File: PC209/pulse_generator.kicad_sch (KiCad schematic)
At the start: 33 parts, among them Q1 BC848W, Q2 BC848W, Q3 BC848W, Q4 BC848W, Q5 BC848W, Q6 BC848W, Q7 BC848W

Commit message: PC209: Initial layout for pulse generator sections
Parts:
- TP1, TP3: footprint TestPoint:TestPoint_Keystone_5015_Micro-Minature -> TestPoint:TestPoint_THTPad_2.0x2.0mm_Drill1.0mm; now left out of the parts list
- TP2: value 10 us delay -> 10 μs delay; footprint TestPoint:TestPoint_Keystone_5015_Micro-Minature -> TestPoint:TestPoint_THTPad_2.0x2.0mm_Drill1.0mm; now left out of the parts list
- TP4: value 10 us delay -> 100 μs pulse; footprint TestPoint:TestPoint_Keystone_5015_Micro-Minature -> TestPoint:TestPoint_THTPad_2.0x2.0mm_Drill1.0mm; now left out of the parts list
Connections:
- net Output: now also TP4.1
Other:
- note added: "10 μs Delay"
- note added: "100 μs Pulse"
- note removed: "10 us Delay"
- note removed: "100 us Pulse"
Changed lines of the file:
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@@
+    (stroke (width 0) (type default) (color 0 0 0 0))
+  )
+  (wire (pts (xy 104.14 104.14) (xy 104.14 110.49))
     (stroke (width 0) (type default) (color 0 0 0 0))
   )
@@
     (stroke (width 0) (type default) (color 0 0 0 0))
   )
-  (text "10 us Delay" (at 52.07 31.75 0)
+  (text "10 μs Delay" (at 52.07 31.75 0)
     (effects (font (size 3 3)) (justify left bottom))
   )
-  (text "100 us Pulse" (at 52.07 95.25 0)
+  (text "100 μs Pulse" (at 52.07 95.25 0)
     (effects (font (size 3 3)) (justify left bottom))
   )
@@
   )
   (symbol (lib_id "Connector:TestPoint") (at 46.99 58.42 0) (unit 1)
-    (in_bom yes) (on_board yes)
+    (in_bom no) (on_board yes)
     (property "Reference" "TP1" (id 0) (at 44.45 57.15 90)
       (effects (font (size 1.27 1.27)) (justify left))
@@
       (effects (font (size 1.27 1.27)) (justify left bottom))
     )
-    (property "Footprint" "TestPoint:TestPoint_Keystone_5015_Micro-Minature" (id 2) (at 52.07 58.42 0)
+    (property "Footprint" "TestPoint:TestPoint_THTPad_2.0x2.0mm_Drill1.0mm" (id 2) (at 52.07 58.42 0)
       (effects (font (size 1.27 1.27)) hide)
     )
@@
   )
   (symbol (lib_id "Connector:TestPoint") (at 104.14 104.14 0) (unit 1)
-    (in_bom yes) (on_board yes)
+    (in_bom no) (on_board yes)
     (property "Reference" "TP4" (id 0) (at 101.6 102.87 90)
       (effects (font (size 1.27 1.27)) (justify left))
     )
-    (property "Value" "10 us delay" (id 1) (at 106.68 102.87 90)
+    (property "Value" "100 μs pulse" (id 1) (at 106.68 102.87 90)
       (effects (font (size 1.27 1.27)) (justify left bottom))
     )
-    (property "Footprint" "TestPoint:TestPoint_Keystone_5015_Micro-Minature" (id 2) (at 109.22 104.14 0)
+    (property "Footprint" "TestPoint:TestPoint_THTPad_2.0x2.0mm_Drill1.0mm" (id 2) (at 109.22 104.14 0)
       (effects (font (size 1.27 1.27)) hide)
     )
@@
   )
   (symbol (lib_id "Connector:TestPoint") (at 101.6 54.61 0) (unit 1)
-    (in_bom yes) (on_board yes)
+    (in_bom no) (on_board yes)
     (property "Reference" "TP3" (id 0) (at 99.06 53.34 90)
       (effects (font (size 1.27 1.27)) (justify left))
@@
       (effects (font (size 1.27 1.27)) (justify left bottom))
     )
-    (property "Footprint" "TestPoint:TestPoint_Keystone_5015_Micro-Minature" (id 2) (at 106.68 54.61 0)
+    (property "Footprint" "TestPoint:TestPoint_THTPad_2.0x2.0mm_Drill1.0mm" (id 2) (at 106.68 54.61 0)
       (effects (font (size 1.27 1.27)) hide)
     )
@@
   )
   (symbol (lib_id "Connector:TestPoint") (at 57.15 101.6 270) (unit 1)
-    (in_bom yes) (on_board yes)
+    (in_bom no) (on_board yes)
     (property "Reference" "TP2" (id 0) (at 58.42 99.06 90)
       (effects (font (size 1.27 1.27)) (justify left))
     )
-    (property "Value" "10 us delay" (id 1) (at 58.42 104.14 90)
+    (property "Value" "10 μs delay" (id 1) (at 58.42 104.14 90)
       (effects (font (size 1.27 1.27)) (justify left bottom))
     )
-    (property "Footprint" "TestPoint:TestPoint_Keystone_5015_Micro-Minature" (id 2) (at 57.15 106.68 0)
-      (effects (font (size 1.27 1.27)) hide)
-    )
+    (property "Footprint" "TestPoint:TestPoint_THTPad_2.0x2.0mm_Drill1.0mm" (id 2) (at 57.15 106.68 0)
+      (effects (font (size 1.27 1.27)) hide)
+    )

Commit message: PC209: Rev 1.0
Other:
- company: (none) -> Peter Farley
- title: (none) -> PC209 Pulse Generator
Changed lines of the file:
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@@
 (kicad_sch (version 20211123) (generator eeschema)
   (paper "A4")
+  (title_block
+    (title "PC209 Pulse Generator")
+    (date "2023-01-16")
+    (rev "1.0")
+    (company "Peter Farley")
+    (comment 1 "Rev 1.0: Initial Design")
+  )
   (junction (at 83.82 113.03) (diameter 0) (color 0 0 0 0)
   )
@@
     (stroke (width 0) (type default) (color 0 0 0 0))
   )
-  (wire (pts (xy 26.67 21.59) (xy 29.21 21.59))
-    (stroke (width 0) (type default) (color 0 0 0 0))
-  )
   (wire (pts (xy 67.31 57.15) (xy 67.31 58.42))
     (stroke (width 0) (type default) (color 0 0 0 0))
@@
     (stroke (width 0) (type default) (color 0 0 0 0))
   )
-  (wire (pts (xy 29.21 19.05) (xy 26.67 19.05))
-    (stroke (width 0) (type default) (color 0 0 0 0))
-  )
   (wire (pts (xy 104.14 110.49) (xy 111.76 110.49))
     (stroke (width 0) (type default) (color 0 0 0 0))
@@
   )
   (wire (pts (xy 57.15 63.5) (xy 59.69 63.5))
-    (stroke (width 0) (type default) (color 0 0 0 0))
-  )
-  (wire (pts (xy 29.21 24.13) (xy 26.67 24.13))
     (stroke (width 0) (type default) (color 0 0 0 0))
   )
@@
     (effects (font (size 3 3)) (justify left bottom))
   )
-  (hierarchical_label "GND" (shape input) (at 26.67 24.13 180)
-    (effects (font (size 1.27 1.27)) (justify right))
-  )
   (hierarchical_label "Output" (shape output) (at 153.67 130.81 0)
     (effects (font (size 1.27 1.27)) (justify left))
   )
-  (hierarchical_label "3.6 V" (shape input) (at 26.67 21.59 180)
-    (effects (font (size 1.27 1.27)) (justify right))
-  )
   (hierarchical_label "Input" (shape input) (at 41.91 63.5 180)
-    (effects (font (size 1.27 1.27)) (justify right))
-  )
-  (hierarchical_label "15 V" (shape input) (at 26.67 19.05 180)
     (effects (font (size 1.27 1.27)) (justify right))
   )
@@
     (pin "2")
   )
-  (symbol (lib_id "lib_symbols:+3.6V") (at 29.21 21.59 270) (unit 1)
-    (in_bom yes) (on_board yes) (fields_autoplaced)
-    (property "Reference" "#PWR0118" (id 0) (at 25.4 21.59 0)
-      (effects (font (size 1.27 1.27)) hide)
-    )
-    (property "Value" "+3.6V" (id 1) (at 33.02 21.5899 90)
-      (effects (font (size 1.27 1.27)) (justify left))
-    )
-    (property "Footprint" "" (id 2) (at 29.21 21.59 0)
-      (effects (font (size 1.27 1.27)) hide)
-    )
-    (property "Datasheet" "" (id 3) (at 29.21 21.59 0)
-      (effects (font (size 1.27 1.27)) hide)
-    )
-    (pin "1")
-  )
   (symbol (lib_id "Device:R_Small") (at 171.45 48.26 90) (unit 1)
     (in_bom yes) (on_board yes)
@@
     (pin "1")
     (pin "2")
-  )
-  (symbol (lib_id "power:+15V") (at 29.21 19.05 270) (unit 1)
-    (in_bom yes) (on_board yes) (fields_autoplaced)
-    (property "Reference" "#PWR0117" (id 0) (at 25.4 19.05 0)
-      (effects (font (size 1.27 1.27)) hide)
-    )
-    (property "Value" "+15V" (id 1) (at 33.02 19.0501 90)
-      (effects (font (size 1.27 1.27)) (justify left))
-    )
-    (property "Footprint" "" (id 2) (at 29.21 19.05 0)
-      (effects (font (size 1.27 1.27)) hide)
-    )
-    (property "Datasheet" "" (id 3) (at 29.21 19.05 0)
-      (effects (font (size 1.27 1.27)) hide)
-    )
-    (pin "1")
   )
   (symbol (lib_id "Transistor_BJT:BC848W") (at 181.61 48.26 0) (unit 1)
@@
     (pin "2")
   )
-  (symbol (lib_id "power:GND") (at 29.21 24.13 90) (unit 1)
-    (in_bom yes) (on_board yes) (fields_autoplaced)
-    (property "Reference" "#PWR0119" (id 0) (at 35.56 24.13 0)
-      (effects (font (size 1.27 1.27)) hide)
-    )
-    (property "Value" "GND" (id 1) (at 33.02 24.1301 90)
-      (effects (font (size 1.27 1.27)) (justify right))
-    )
-    (property "Footprint" "" (id 2) (at 29.21 24.13 0)
-      (effects (font (size 1.27 1.27)) hide)
-    )
-    (property "Datasheet" "" (id 3) (at 29.21 24.13 0)
-      (effects (font (size 1.27 1.27)) hide)
-    )
-    (pin "1")
-  )
   (symbol (lib_id "Device:R_Small") (at 83.82 105.41 180) (unit 1)

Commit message: PC209: Fix silkscreen error, backannotate to schematic.
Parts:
- renumbered C2 to C1, C4 to C3, C6 to C4, C1 to C5, C3 to C6, C5 to C7, Q6 to Q10, Q7 to Q11, Q5 to Q12, Q3 to Q13, Q2 to Q14, Q4 to Q15, Q1 to Q2, R4 to R11, R9 to R2, R18 to R20, R14 to R21, R13 to R22, R17 to R23, R8 to R24, R12 to R25, R16 to R26, R19 to R27, R5 to R28, R15 to R29, R10 to R30, R7 to R33, R11 to R34, R6 to R9, TP2 to TP5, TP3 to TP6, TP1 to TP7

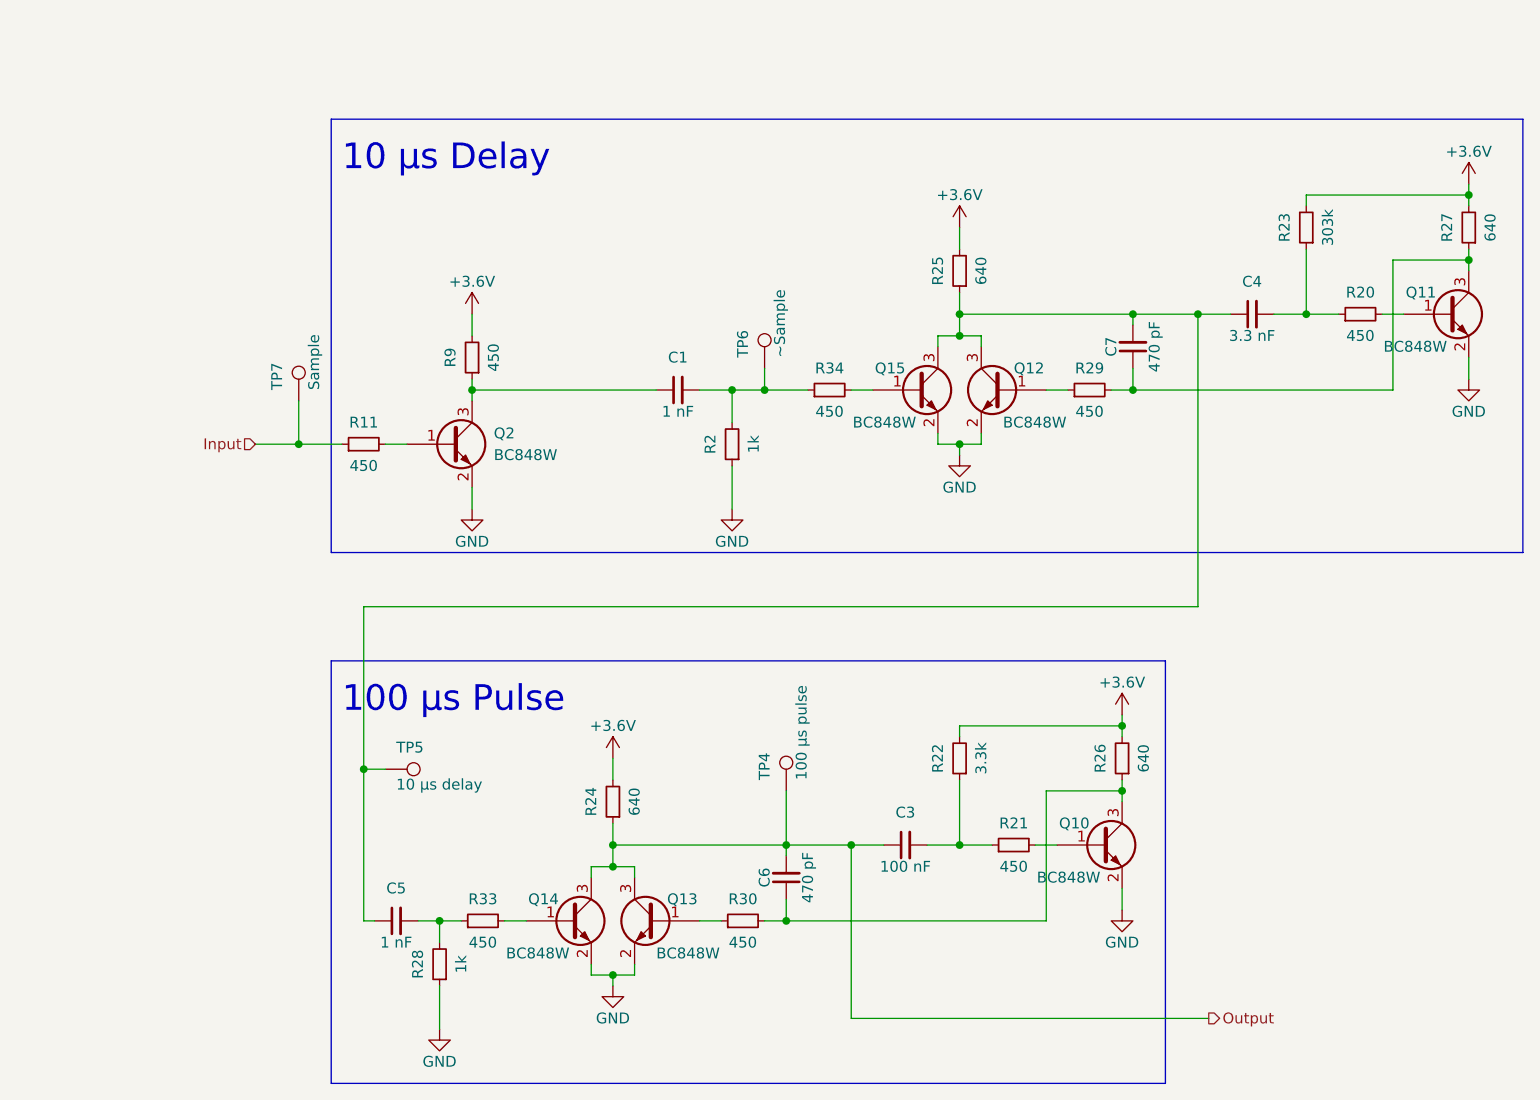
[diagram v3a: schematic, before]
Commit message: PC209: Fix position of -15 V and +3.6 V on card edge
Update component values
Make library path relative
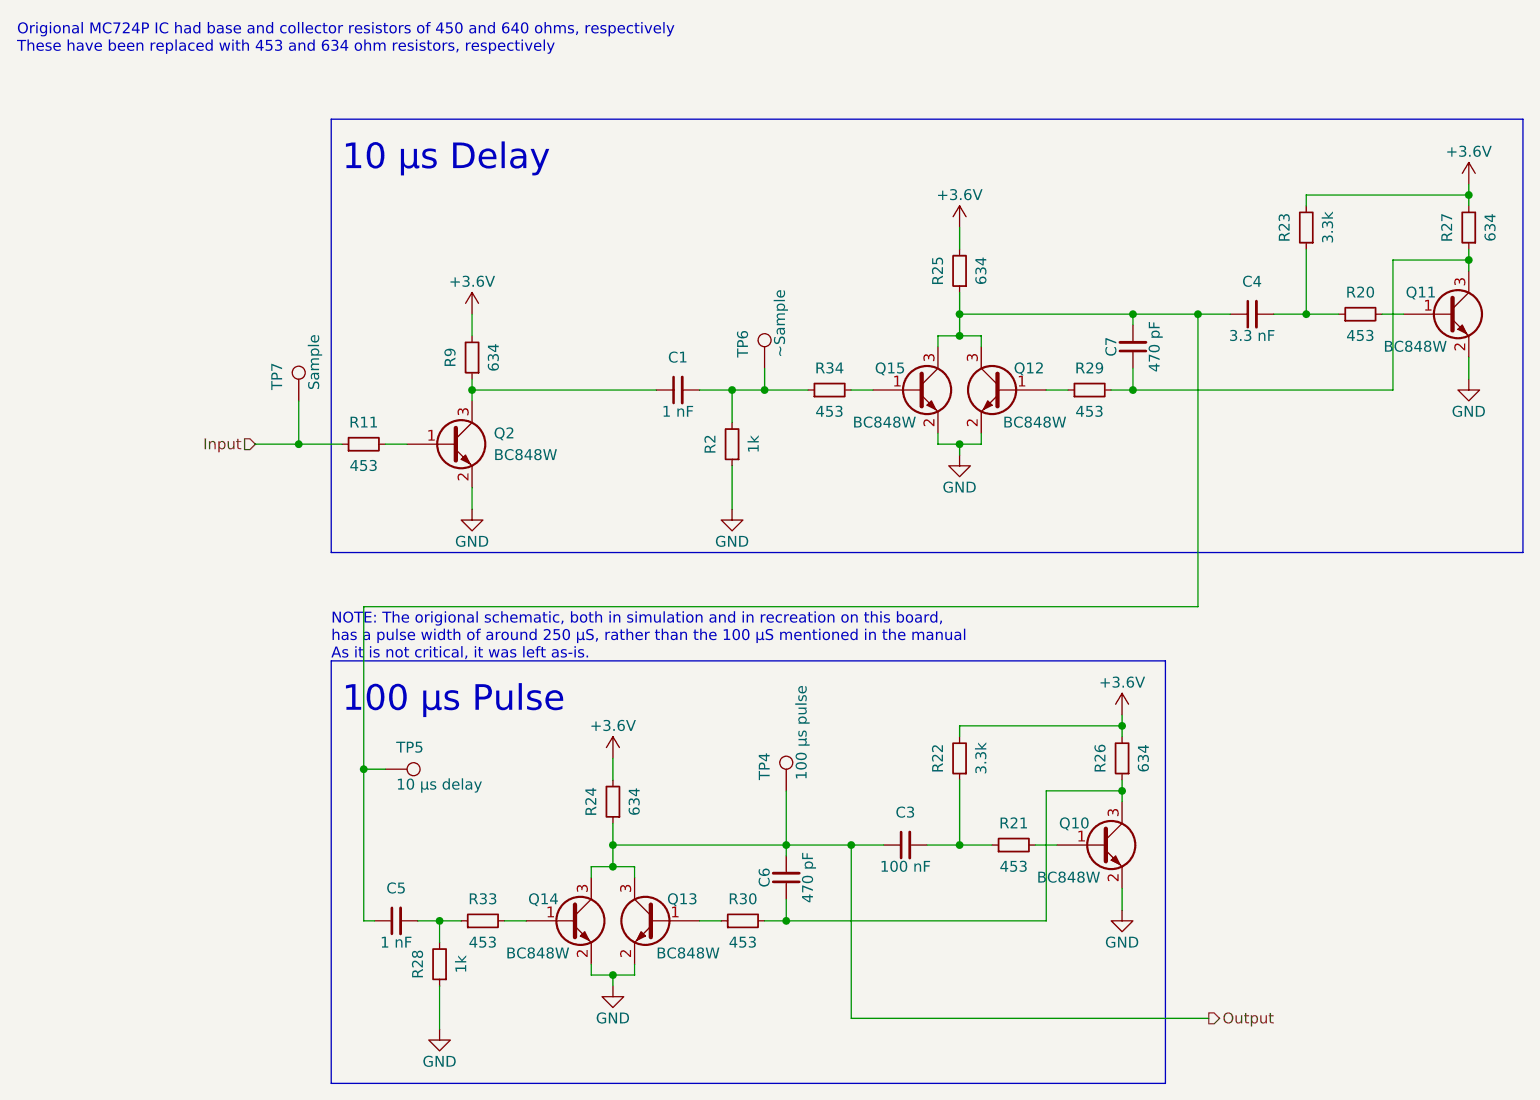
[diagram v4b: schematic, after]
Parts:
- R11, R20, R21, R29, R30, R33, R34: value 450 -> 453
- R23: value 303k -> 3.3k
- R24, R25, R26, R27: value 640 -> 634
- R9: value 450 -> 634
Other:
- note added: "NOTE: The origional schematic, both in simulation and in recreation on this board, has a pulse width of around 250 μS, rather than the 100 μS mentioned in the manual As it is not critical, it was left as-is."
- note added: "Origional MC724P IC had base and collector resistors of 450 and 640 ohms, respectively These have been replaced with 453 and 634 ohm resistors, respectively"
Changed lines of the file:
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@@
   (title_block
     (title "PC209 Pulse Generator")
-    (date "2023-01-16")
-    (rev "1.0")
+    (date "2023-01-31")
+    (rev "1.1")
     (company "Peter Farley")
     (comment 1 "Rev 1.0: Initial Design")
+    (comment 2 "Rev 1.1: Fix pinout of card edge, update component values")
   )
   (junction (at 83.82 113.03) (diameter 0) (color 0 0 0 0)
@@
   (wire (pts (xy 165.1 34.29) (xy 184.15 34.29))
     (stroke (width 0) (type default) (color 0 0 0 0))
+  )
+  (text "NOTE: The origional schematic, both in simulation and in recreation on this board,\nhas a pulse width of around 250 μS, rather than the 100 μS mentioned in the manual\nAs it is not critical, it was left as-is."
+    (at 50.8 88.9 0)
+    (effects (font (size 1.27 1.27)) (justify left bottom))
   )
   (text "10 μs Delay" (at 52.07 31.75 0)
@@
   (text "100 μs Pulse" (at 52.07 95.25 0)
     (effects (font (size 3 3)) (justify left bottom))
+  )
+  (text "Origional MC724P IC had base and collector resistors of 450 and 640 ohms, respectively\nThese have been replaced with 453 and 634 ohm resistors, respectively"
+    (at 13.97 17.78 0)
+    (effects (font (size 1.27 1.27)) (justify left bottom))
   )
   (hierarchical_label "Output" (shape output) (at 153.67 130.81 0)
@@
     (in_bom yes) (on_board yes)
     (property "Reference" "R20" (id 0) (at 171.45 45.72 90))
-    (property "Value" "450" (id 1) (at 171.45 50.8 90))
+    (property "Value" "453" (id 1) (at 171.45 50.8 90))
     (property "Footprint" "Resistor_SMD:R_0603_1608Metric" (id 2) (at 171.45 48.26 0)
       (effects (font (size 1.27 1.27)) hide)
@@
     (in_bom yes) (on_board yes)
     (property "Reference" "R27" (id 0) (at 181.61 38.1 90))
-    (property "Value" "640" (id 1) (at 186.69 38.1 90))
+    (property "Value" "634" (id 1) (at 186.69 38.1 90))
     (property "Footprint" "Resistor_SMD:R_0603_1608Metric" (id 2) (at 184.15 38.1 0)
       (effects (font (size 1.27 1.27)) hide)
@@
     (in_bom yes) (on_board yes)
     (property "Reference" "R33" (id 0) (at 68.58 116.84 90))
-    (property "Value" "450" (id 1) (at 68.58 121.92 90))
+    (property "Value" "453" (id 1) (at 68.58 121.92 90))
     (property "Footprint" "Resistor_SMD:R_0603_1608Metric" (id 2) (at 68.58 119.38 0)
       (effects (font (size 1.27 1.27)) hide)
@@
     (in_bom yes) (on_board yes)
     (property "Reference" "R30" (id 0) (at 99.06 116.84 90))
-    (property "Value" "450" (id 1) (at 99.06 121.92 90))
+    (property "Value" "453" (id 1) (at 99.06 121.92 90))
     (property "Footprint" "Resistor_SMD:R_0603_1608Metric" (id 2) (at 99.06 119.38 0)
       (effects (font (size 1.27 1.27)) hide)
@@
     (in_bom yes) (on_board yes)
     (property "Reference" "R29" (id 0) (at 139.7 54.61 90))
-    (property "Value" "450" (id 1) (at 139.7 59.69 90))
+    (property "Value" "453" (id 1) (at 139.7 59.69 90))
     (property "Footprint" "Resistor_SMD:R_0603_1608Metric" (id 2) (at 139.7 57.15 0)
       (effects (font (size 1.27 1.27)) hide)
@@
     (in_bom yes) (on_board yes)
     (property "Reference" "R26" (id 0) (at 140.97 100.33 90))
-    (property "Value" "640" (id 1) (at 146.05 100.33 90))
+    (property "Value" "634" (id 1) (at 146.05 100.33 90))
     (property "Footprint" "Resistor_SMD:R_0603_1608Metric" (id 2) (at 143.51 100.33 0)
       (effects (font (size 1.27 1.27)) hide)
@@
     (in_bom yes) (on_board yes)
     (property "Reference" "R24" (id 0) (at 81.28 105.41 90))
-    (property "Value" "640" (id 1) (at 86.36 105.41 90))
+    (property "Value" "634" (id 1) (at 86.36 105.41 90))
     (property "Footprint" "Resistor_SMD:R_0603_1608Metric" (id 2) (at 83.82 105.41 0)
       (effects (font (size 1.27 1.27)) hide)
@@
     (in_bom yes) (on_board yes)
     (property "Reference" "R9" (id 0) (at 64.77 53.34 90))
-    (property "Value" "450" (id 1) (at 69.85 53.34 90))
+    (property "Value" "634" (id 1) (at 69.85 53.34 90))
     (property "Footprint" "Resistor_SMD:R_0603_1608Metric" (id 2) (at 67.31 53.34 0)
       (effects (font (size 1.27 1.27)) hide)
@@
     (in_bom yes) (on_board yes)
     (property "Reference" "R25" (id 0) (at 121.92 43.18 90))
-    (property "Value" "640" (id 1) (at 127 43.18 90))
+    (property "Value" "634" (id 1) (at 127 43.18 90))
     (property "Footprint" "Resistor_SMD:R_0603_1608Metric" (id 2) (at 124.46 43.18 0)
       (effects (font (size 1.27 1.27)) hide)
@@
     (in_bom yes) (on_board yes)
     (property "Reference" "R34" (id 0) (at 109.22 54.61 90))
-    (property "Value" "450" (id 1) (at 109.22 59.69 90))
+    (property "Value" "453" (id 1) (at 109.22 59.69 90))
     (property "Footprint" "Resistor_SMD:R_0603_1608Metric" (id 2) (at 109.22 57.15 0)
       (effects (font (size 1.27 1.27)) hide)
@@
     (in_bom yes) (on_board yes)
     (property "Reference" "R23" (id 0) (at 162.56 38.1 90))
-    (property "Value" "303k" (id 1) (at 167.64 38.1 90))
+    (property "Value" "3.3k" (id 1) (at 167.64 38.1 90))
     (property "Footprint" "Resistor_SMD:R_0603_1608Metric" (id 2) (at 165.1 38.1 0)
       (effects (font (size 1.27 1.27)) hide)
@@
     (in_bom yes) (on_board yes)
     (property "Reference" "R21" (id 0) (at 130.81 107.95 90))
-    (property "Value" "450" (id 1) (at 130.81 113.03 90))
+    (property "Value" "453" (id 1) (at 130.81 113.03 90))
     (property "Footprint" "Resistor_SMD:R_0603_1608Metric" (id 2) (at 130.81 110.49 0)
       (effects (font (size 1.27 1.27)) hide)
@@
     (in_bom yes) (on_board yes)
     (property "Reference" "R11" (id 0) (at 54.61 60.96 90))
-    (property "Value" "450" (id 1) (at 54.61 66.04 90))
+    (property "Value" "453" (id 1) (at 54.61 66.04 90))
     (property "Footprint" "Resistor_SMD:R_0603_1608Metric" (id 2) (at 54.61 63.5 0)
       (effects (font (size 1.27 1.27)) hide)
